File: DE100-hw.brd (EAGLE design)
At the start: 96.5 x 71.8 mm, 51 parts, among them IC3 74HC14D, IC4 74HC14D, U1 TLP521-4(GB), U2 TLP521-4(GB), X1 22-23-2041, X2 22-23-2031, X3 22-23-2101

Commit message: post production revision
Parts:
- R1, R10, R11, R18, R2, R26, R27, R3, R4, R9: value (none) -> 330
- R12, R13, R14, R5, R6, R7, R8: value (none) -> 10k
- R15, R16, R17, R19, R20, R21, R22, R23, R24, R25: value (none) -> 1k
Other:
- board text added: "Designed by:"

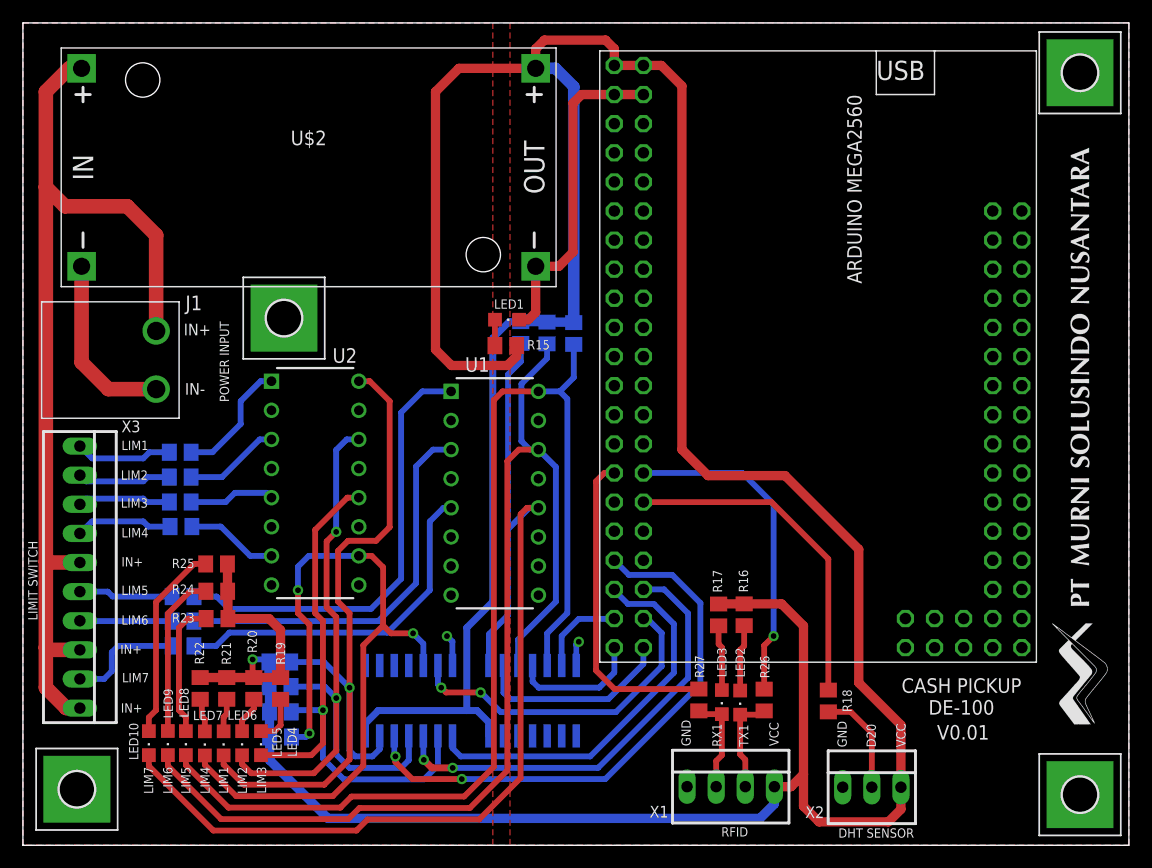
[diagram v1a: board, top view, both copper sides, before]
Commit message: change molex connector library
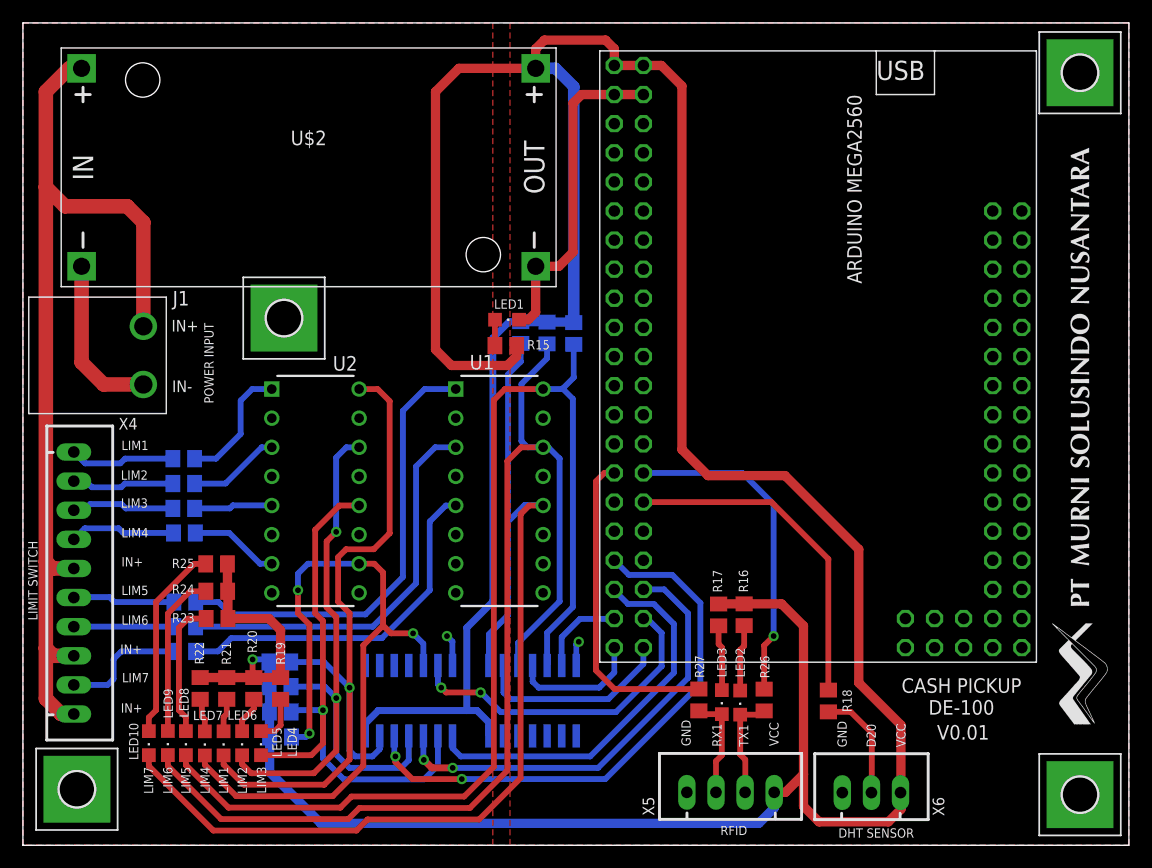
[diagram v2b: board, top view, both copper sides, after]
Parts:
- removed X1: 22-23-2041, con-molex:22-23-2041
- removed X2: 22-23-2031, con-molex:22-23-2031
- removed X3: 22-23-2101, con-molex:22-23-2101
- added X4: JST-XH-10-PIN-LONG-PAD, Rembrandt Electronics - JST XH Connectors v1-0:JST-XH-10-PACKAGE-LONG-PAD
- added X5: JST-XH-04-PIN-LONG-PAD, Rembrandt Electronics - JST XH Connectors v1-0:JST-XH-04-PACKAGE-LONG-PAD
- added X6: JST-XH-03-PIN-LONG-PAD, Rembrandt Electronics - JST XH Connectors v1-0:JST-XH-03-PACKAGE-LONG-PAD
- moved J1 1.19 mm to (43.5, 51.0)
- moved U2 0.69 mm to (58.5, 41.7)
- moved R1 0.64 mm to (47.0, 44.5)
- moved R2 0.64 mm to (47.0, 42.3)
- moved R3 0.64 mm to (47.0, 40.1)
- moved R4 0.64 mm to (47.1, 38.0)
- moved R10 0.51 mm to (47.1, 29.8)
- moved R11 0.51 mm to (47.1, 27.7)
- moved R9 0.51 mm to (47.1, 32.0)
- moved U1 0.45 mm to (74.6, 41.7)
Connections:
- net +5V: now also X5.4, X6.3; no longer X1.4, X2.3
- net GND: now also X5.1, X6.1; no longer X1.1, X2.1
- net LS-1: now also X4.1; no longer X3.1
- net LS-2: now also X4.2; no longer X3.2
- net LS-3: now also X4.3; no longer X3.3
- net LS-4: now also X4.4; no longer X3.4
- net LS-5: now also X4.6; no longer X3.6
- net LS-6: now also X4.7; no longer X3.7
- net LS-7: now also X4.9; no longer X3.9
- net N$35: now also X5.3; no longer X1.3
- net N$36: now also X5.2; no longer X1.2
- net N$38: now also X6.2; no longer X2.2
- net VCC-ISO: now also X4.10, X4.5, X4.8; no longer X3.10, X3.5, X3.8
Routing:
- net LIN-6: track 96.4 -> 97.8 mm
- net GND-ISO: track 15.9 -> 14.6 mm
- net VCC-ISO: track 85.4 -> 84.2 mm
- net LIN-4: track 65.9 -> 64.7 mm
- net +5V: track 330.2 -> 331.1 mm
- net LS-3: track 8.15 -> 9.02 mm
- net LS-2: track 8.18 -> 8.99 mm
- net LS-4: track 8.48 -> 9.27 mm
- net LS-1: track 8.47 -> 9.22 mm
- net LS-7: track 10.2 -> 11.0 mm
- net LS-5: track 8.23 -> 8.93 mm
- net LS-6: track 8.06 -> 8.73 mm
- net N$26: track 7.52 -> 6.85 mm
- net LIN-7: track 95.1 -> 95.7 mm
- net LIN-2: track 57.9 -> 57.3 mm
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
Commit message: change position component and logo HM
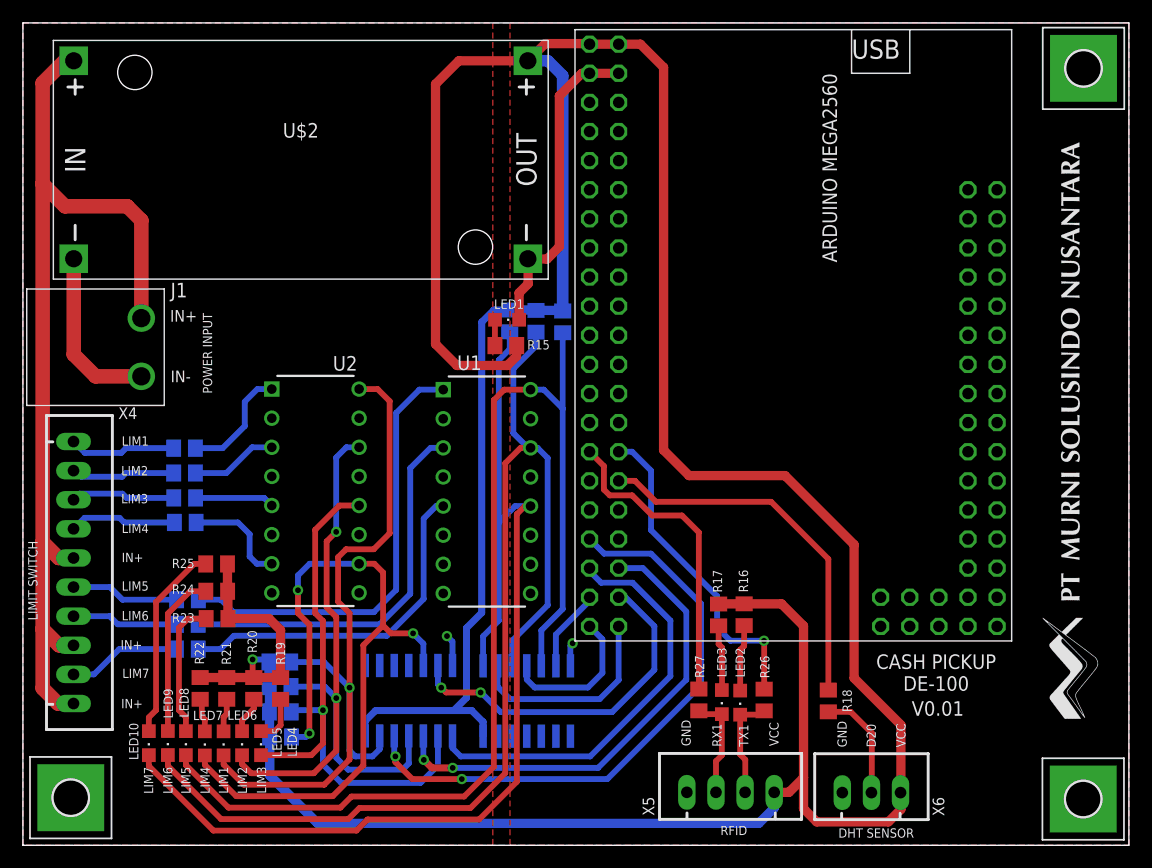
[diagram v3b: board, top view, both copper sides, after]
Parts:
- removed H4: MOUNT-PAD-SQUARE3.0, holes:3,0-PAD-SQUARE
- moved U$1 2.85 mm to (102.8, 46.4)
- moved R12 1.40 mm to (80.1, 56.4)
- moved R13 1.40 mm to (77.8, 56.5)
- moved R14 1.40 mm to (75.5, 56.5)
- moved U1 1.09 mm to (73.5, 41.6)
- moved U$2 0.95 mm to (57.2, 70.6)
- moved R1 0.92 mm to (47.1, 45.4)
- moved R3 0.92 mm to (47.1, 41.1)
- moved R2 0.92 mm to (47.1, 43.2)
- moved R4 0.92 mm to (47.2, 38.9)
- moved X4 0.91 mm to (37.4, 34.5)
- moved H1 0.91 mm to (37.2, 14.9)
- moved J1 0.73 mm to (43.3, 51.7)
- moved IC4 0.51 mm to (77.0, 23.3)
- moved H3 0.49 mm to (125.5, 78.5)
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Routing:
- net LMT-1: track 49.1 -> 52.2 mm
- net DHT: track 29.6 -> 32.6 mm
- net LMT-2: track 39.1 -> 41.9 mm
- net LMT-3: track 34.5 -> 37.2 mm
- net LMT-4: track 28.9 -> 31.0 mm
- net LMT-6: track 11.5 -> 13.1 mm
- net N$27: track 7.79 -> 9.23 mm
- net LIN-6: track 97.8 -> 96.7 mm
- net GND: track 33.9 -> 32.8 mm
- net LS-7: track 11.0 -> 9.90 mm
- net N$33: track 35.2 -> 34.2 mm
- net N$24: track 11.0 -> 10.0 mm
- net N$32: track 39.8 -> 38.9 mm
- net N$34: track 31.5 -> 30.7 mm
- net LIN-5: track 98.8 -> 99.7 mm
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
